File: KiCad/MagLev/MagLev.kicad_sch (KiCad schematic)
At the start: 27 parts, among them J1 Barrel_Jack, Q5 ZX5T1951GTA, U10 DRV5505, U11 DRV5505, U12 DRV5505, U3 L78L05_SO8, U4 TL431A, U5 LM393

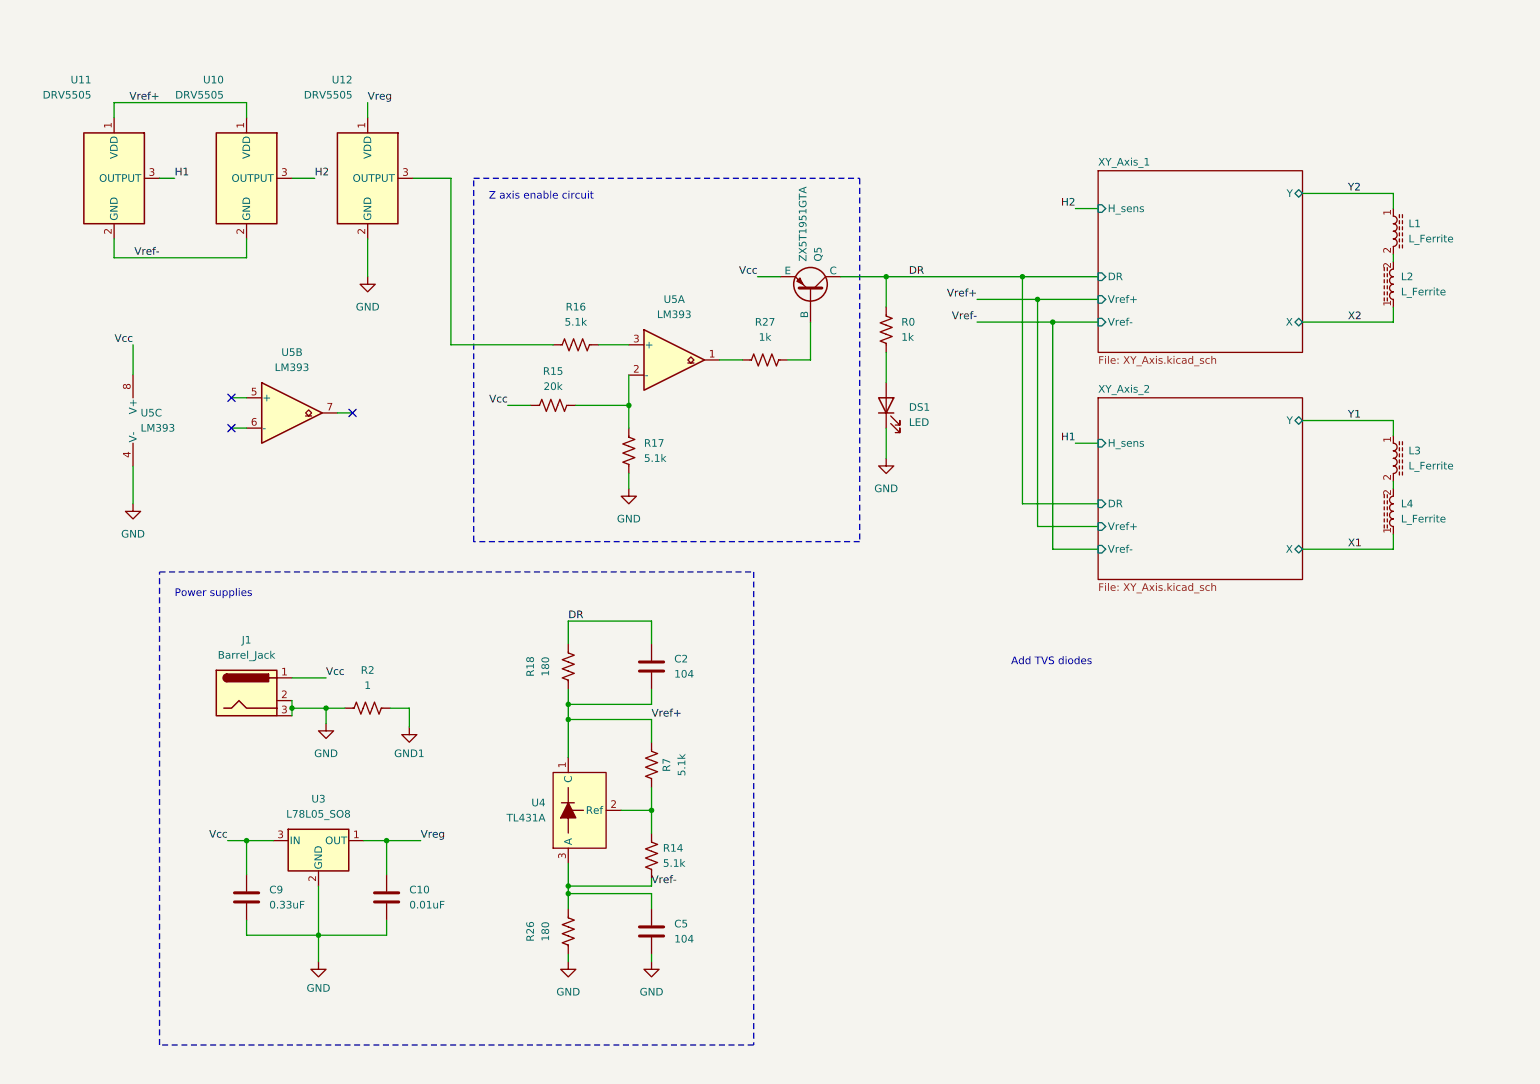
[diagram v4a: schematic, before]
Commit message: Update spice model to match enbs design. Add TVS diodes to schematic.
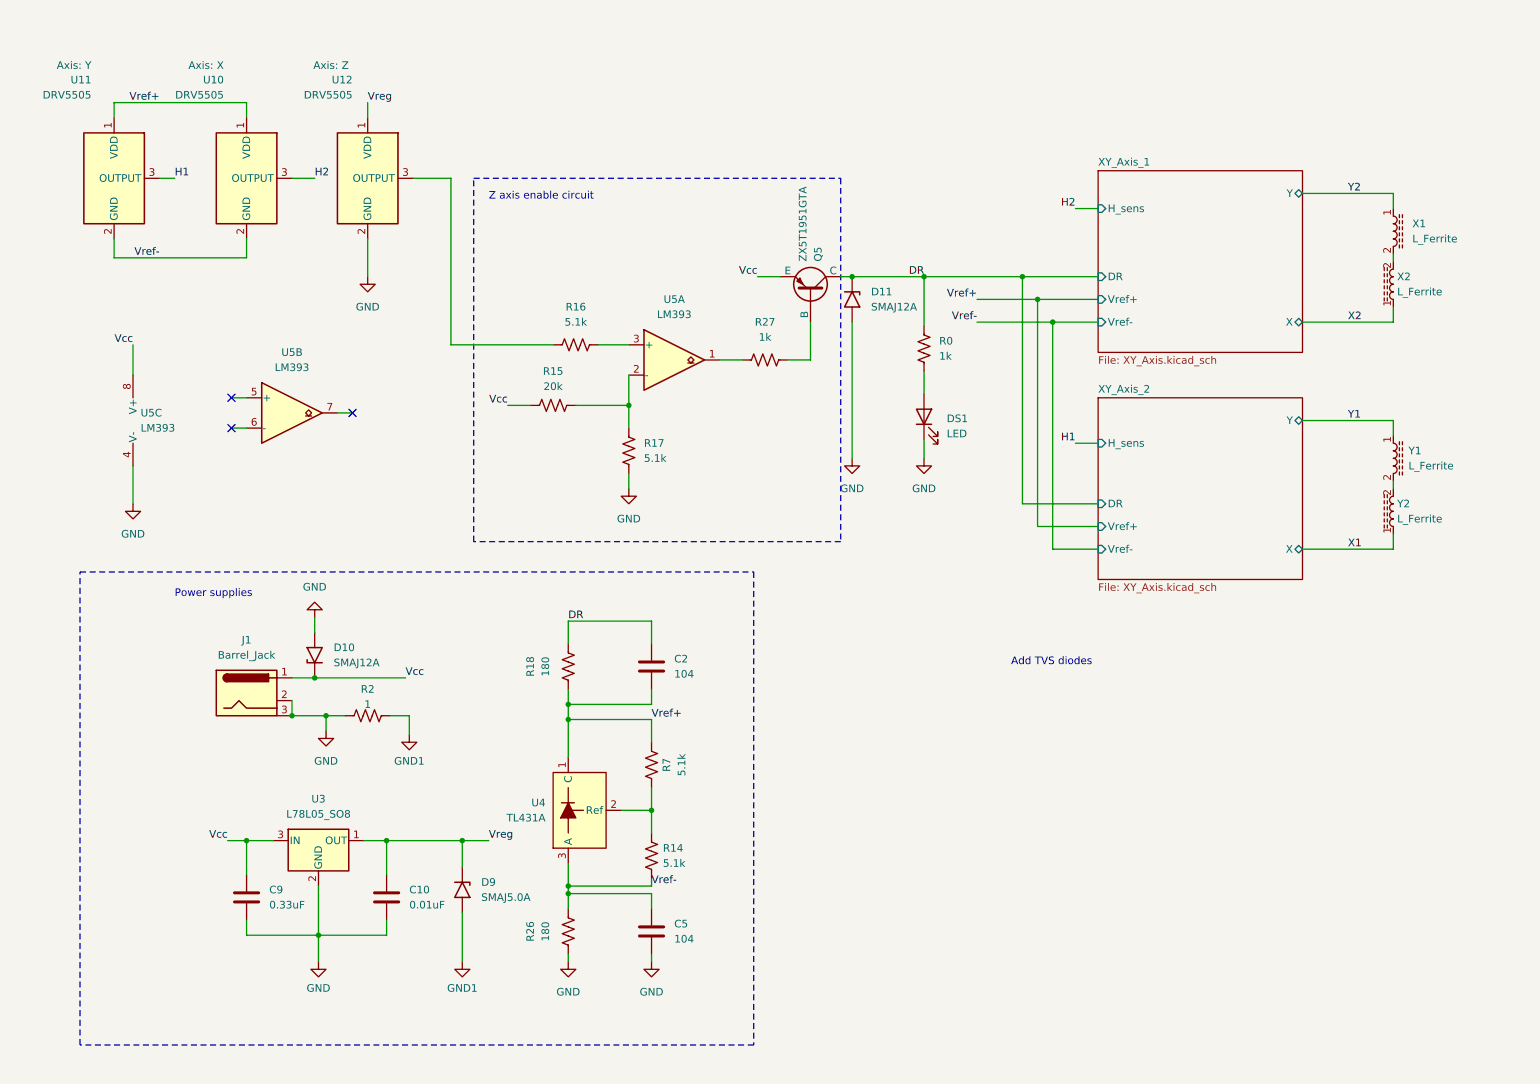
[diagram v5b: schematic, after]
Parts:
- added D10, D11: SMAJ12A, Diode_SMD:D_SMA_Handsoldering, symbol Diode:SMAJ12A
- added D9: SMAJ5.0A, Diode_SMD:D_SMA_Handsoldering, symbol Diode:SMAJ5.0A
- U10: Axis (none) -> X
- U11: Axis (none) -> Y
- U12: Axis (none) -> Z
- renumbered L1 to X1, L2 to X2, L3 to Y1, L4 to Y2
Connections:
- net DR: now also D11.1 (A1)
- net GND: now also D10.2 (A2), D11.2 (A2)
- net GND1: now also D9.2 (A2)
- net Vcc: now also D10.1 (A1)
- net Vreg: now also D9.1 (A1)
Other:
- moved on the sheet: DS1, R0, R2

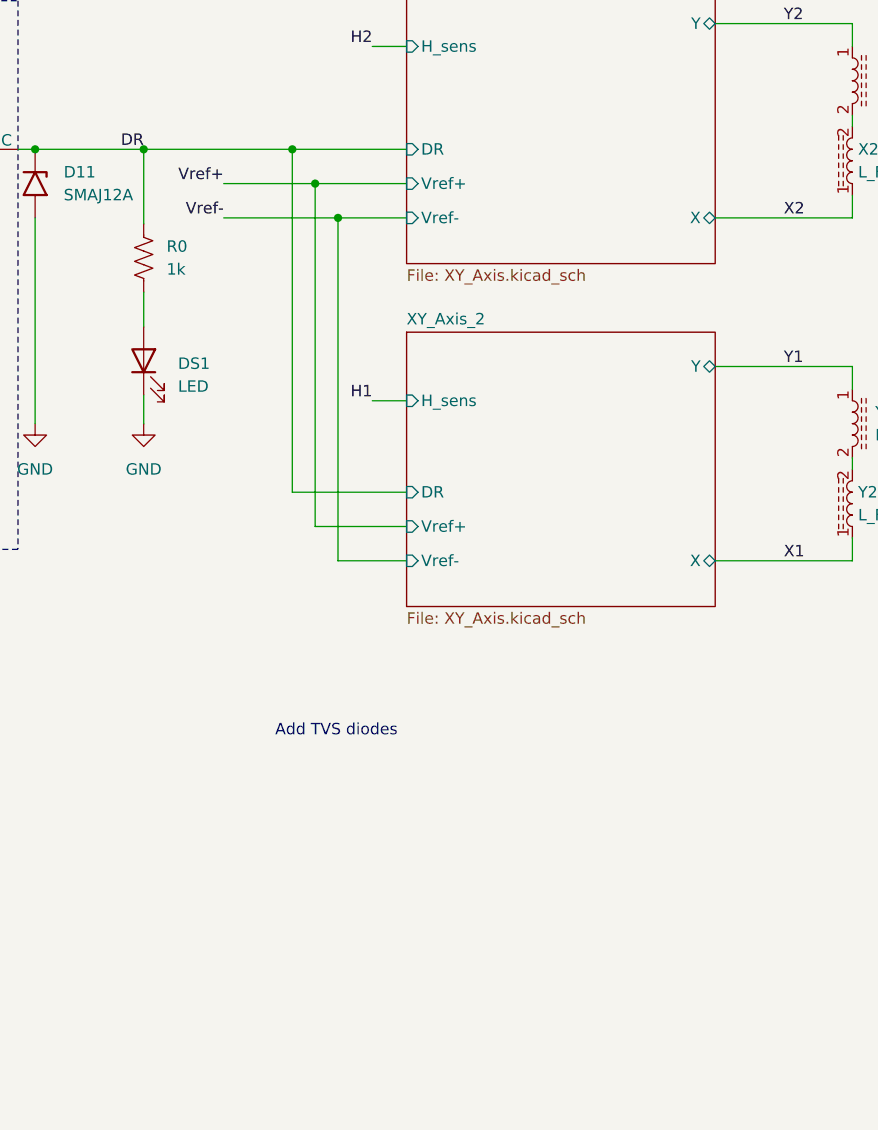
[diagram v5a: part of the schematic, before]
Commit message: Add MCU page to schematic.
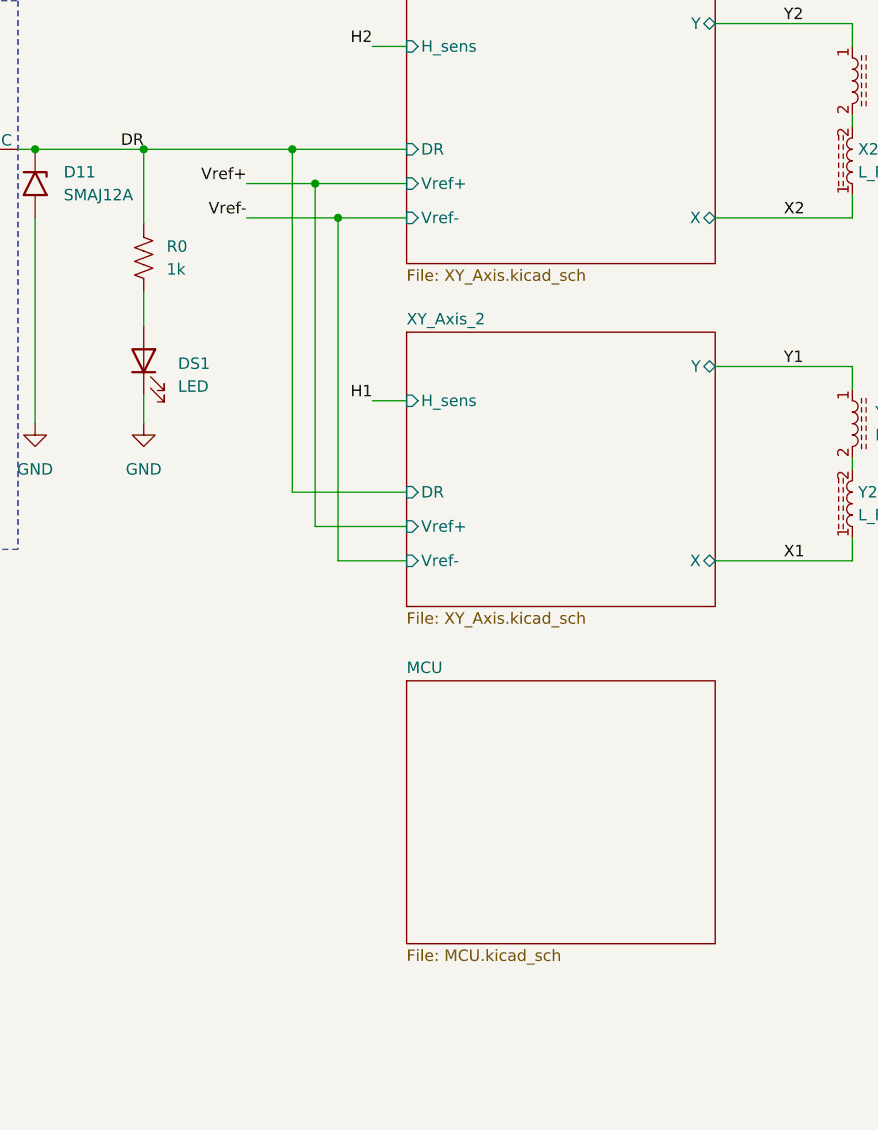
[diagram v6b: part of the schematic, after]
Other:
- added sheet MCU (MCU.kicad_sch)
- note removed: "Add TVS diodes"
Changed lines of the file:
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@@
     (stroke (width 0) (type default))
   )
-  (wire (pts (xy 183.515 66.04) (xy 196.215 66.04))
+  (wire (pts (xy 186.055 66.04) (xy 196.215 66.04))
     (stroke (width 0) (type default))
   )
@@
     (stroke (width 0) (type default))
   )
-  (wire (pts (xy 183.515 62.23) (xy 193.675 62.23))
+  (wire (pts (xy 186.055 62.23) (xy 193.675 62.23))
     (stroke (width 0) (type default))
   )
@@
     (effects (font (size 1.27 1.27)) (justify left bottom))
   )
-  (text "Add TVS diodes" (at 189.23 123.825 0)
-    (effects (font (size 1.27 1.27)) (justify left bottom))
-  )
   (label "Vcc" (at 87.63 125.73 0) (fields_autoplaced)
     (effects (font (size 1.27 1.27)) (justify left bottom))
   )
-  (label "Vref-" (at 183.515 66.04 180) (fields_autoplaced)
+  (label "Vref-" (at 186.055 66.04 180) (fields_autoplaced)
     (effects (font (size 1.27 1.27)) (justify right bottom))
   )
@@
     (effects (font (size 1.27 1.27)) (justify left bottom))
   )
-  (label "Vref+" (at 183.515 62.23 180) (fields_autoplaced)
+  (label "Vref+" (at 186.055 62.23 180) (fields_autoplaced)
     (effects (font (size 1.27 1.27)) (justify right bottom))
   )
@@
       )
     )
+  )
+  (sheet (at 203.835 117.475) (size 34.29 29.21) (fields_autoplaced)
+    (stroke (width 0.1524) (type solid))
+    (fill (color 0 0 0 0.0000))
+    (property "Sheetname" "MCU" (at 203.835 116.7634 0)
+      (effects (font (size 1.27 1.27)) (justify left bottom))
+    )
+    (property "Sheetfile" "MCU.kicad_sch" (at 203.835 147.2696 0)
+      (effects (font (size 1.27 1.27)) (justify left top))
+    )
+    (instances
+      (project "MagLev"
+        (path "/5eab7e8b-54e1-47d0-9dc3-1e7c3fa2f560" (page "4"))
+      )
+    )

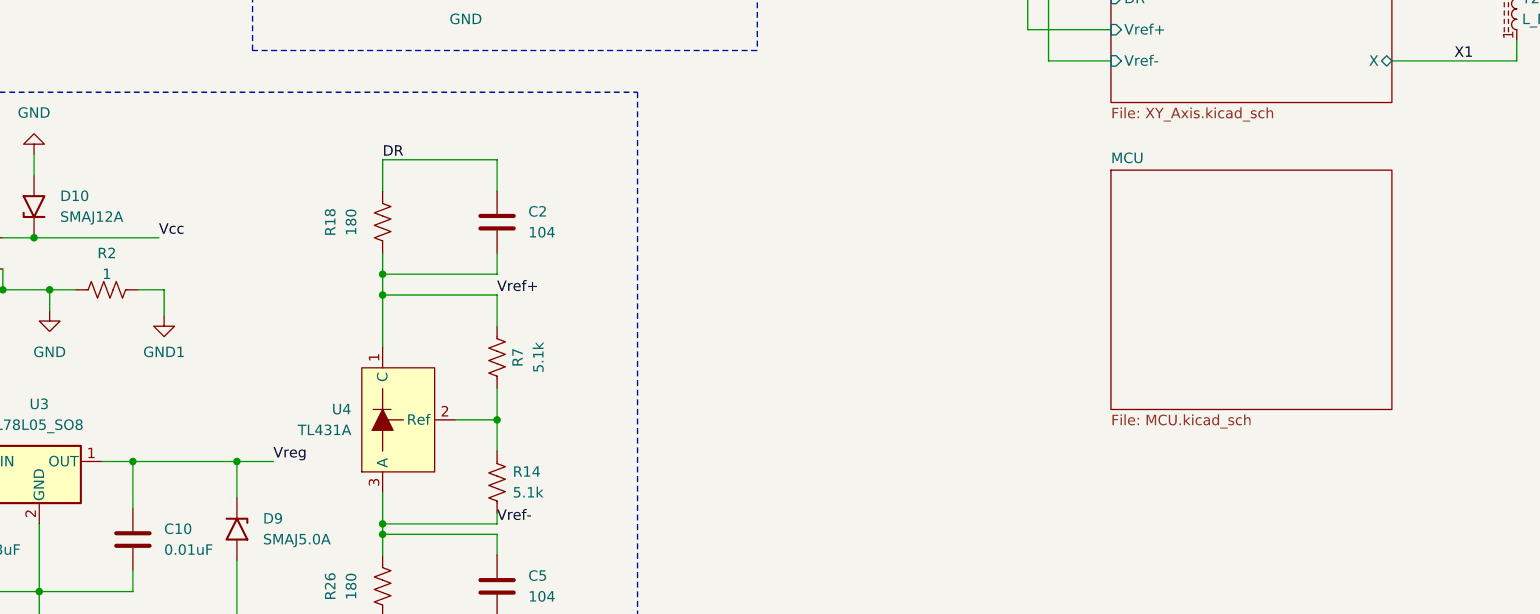
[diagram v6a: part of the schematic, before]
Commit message: Add MCU and FTDI IC to schematic.
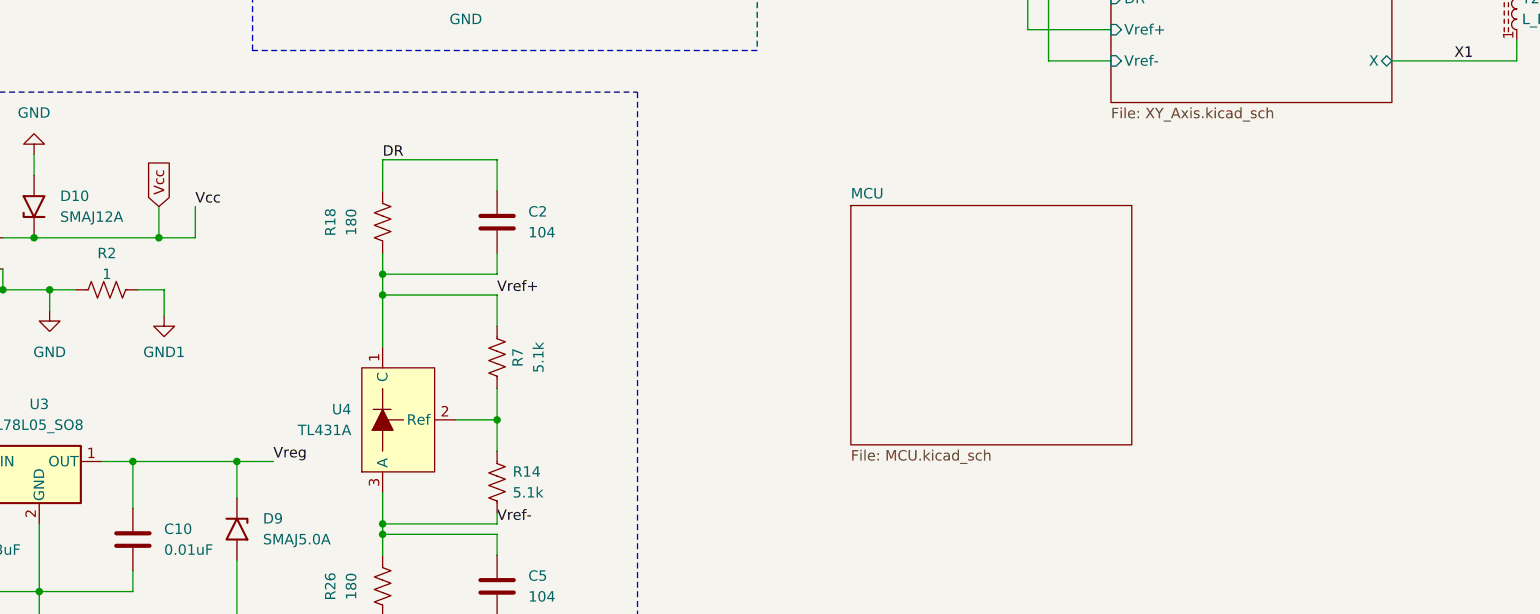
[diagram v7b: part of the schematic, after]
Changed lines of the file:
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@@
   (junction (at 114.935 132.715) (diameter 0) (color 0 0 0 0)
+  )
+  (junction (at 87.63 125.73) (diameter 0) (color 0 0 0 0)
   )
   (junction (at 84.455 153.035) (diameter 0) (color 0 0 0 0)
@@
     (stroke (width 0) (type default))
   )
+  (wire (pts (xy 92.075 125.73) (xy 92.075 121.92))
+    (stroke (width 0) (type default))
+  )
   (wire (pts (xy 97.155 165.1) (xy 97.155 173.355))
     (stroke (width 0) (type default))
@@
     (stroke (width 0) (type default))
   )
+  (wire (pts (xy 87.63 121.92) (xy 87.63 125.73))
+    (stroke (width 0) (type default))
+  )
   (wire (pts (xy 114.935 172.085) (xy 114.935 173.355))
     (stroke (width 0) (type default))
@@
   )
   (wire (pts (xy 73.025 160.655) (xy 73.025 168.91))
+    (stroke (width 0) (type default))
+  )
+  (wire (pts (xy 87.63 125.73) (xy 92.075 125.73))
     (stroke (width 0) (type default))
   )
@@
     (effects (font (size 1.27 1.27)) (justify left bottom))
   )
-  (label "Vcc" (at 87.63 125.73 0) (fields_autoplaced)
+  (label "Vcc" (at 92.075 121.92 0) (fields_autoplaced)
     (effects (font (size 1.27 1.27)) (justify left bottom))
   )
@@
   (label "DR" (at 114.935 116.205 0) (fields_autoplaced)
     (effects (font (size 1.27 1.27)) (justify left bottom))
+  )
+  (global_label "Vcc" (shape input) (at 87.63 121.92 90) (fields_autoplaced)
+    (effects (font (size 1.27 1.27)) (justify left))
+    (property "Intersheetrefs" "${INTERSHEET_REFS}" (at 87.63 115.669 90)
+      (effects (font (size 1.27 1.27)) (justify left) hide)
+    )
   )
   (symbol (lib_id "power:GND1") (at 88.265 135.255 0) (unit 1)
@@
     )
   )
-  (sheet (at 203.835 117.475) (size 34.29 29.21) (fields_autoplaced)
+  (sheet (at 172.085 121.793) (size 34.29 29.21) (fields_autoplaced)
     (stroke (width 0.1524) (type solid))
     (fill (color 0 0 0 0.0000))
-    (property "Sheetname" "MCU" (at 203.835 116.7634 0)
+    (property "Sheetname" "MCU" (at 172.085 121.0814 0)
       (effects (font (size 1.27 1.27)) (justify left bottom))
     )
-    (property "Sheetfile" "MCU.kicad_sch" (at 203.835 147.2696 0)
+    (property "Sheetfile" "MCU.kicad_sch" (at 172.085 151.5876 0)
       (effects (font (size 1.27 1.27)) (justify left top))
     )
